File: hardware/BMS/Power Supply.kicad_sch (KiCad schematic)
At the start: 14 parts, among them U2 LM2596S-ADJ

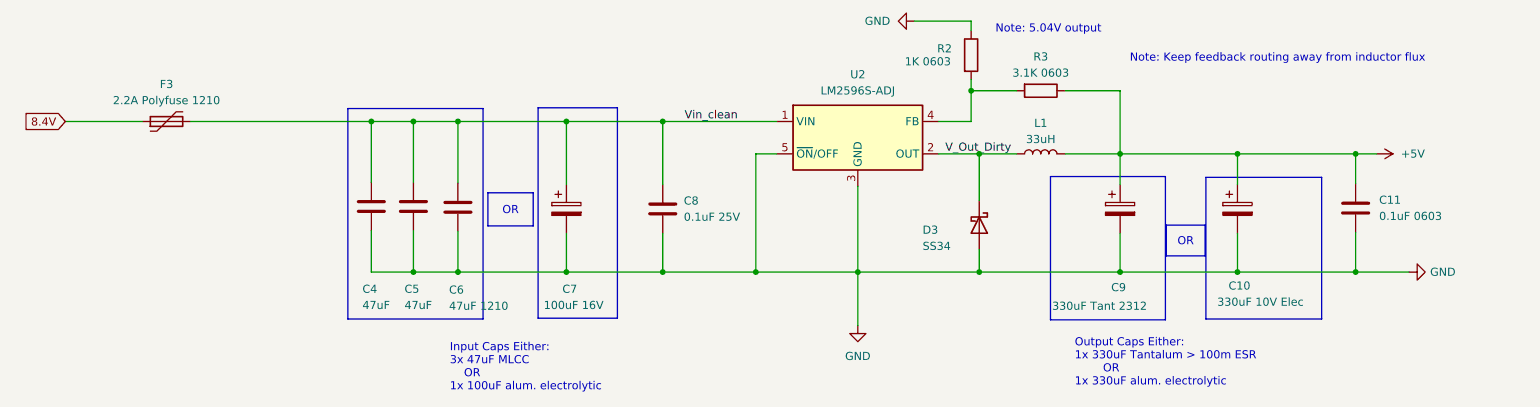
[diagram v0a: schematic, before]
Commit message: Hardware - Controller - Rev 0.3
* Consolidate various asset dirs into single symlinked directory.
* Fixes major flaw with previous atmega328 layout - wrong schematic symbol caused incorrect routing
* Use smaller crystal closer to mcu
* Add QR to silkscreen
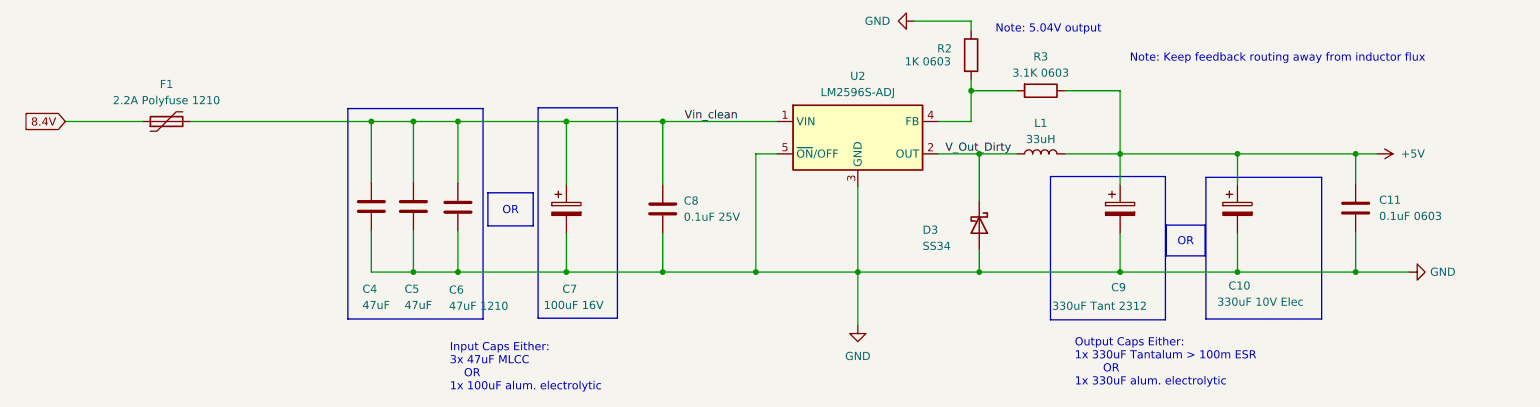
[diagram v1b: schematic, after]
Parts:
- renumbered F3 to F1
